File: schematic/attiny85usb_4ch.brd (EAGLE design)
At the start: 75.2 x 19 mm, 11 parts, among them IC1 PCF8574P

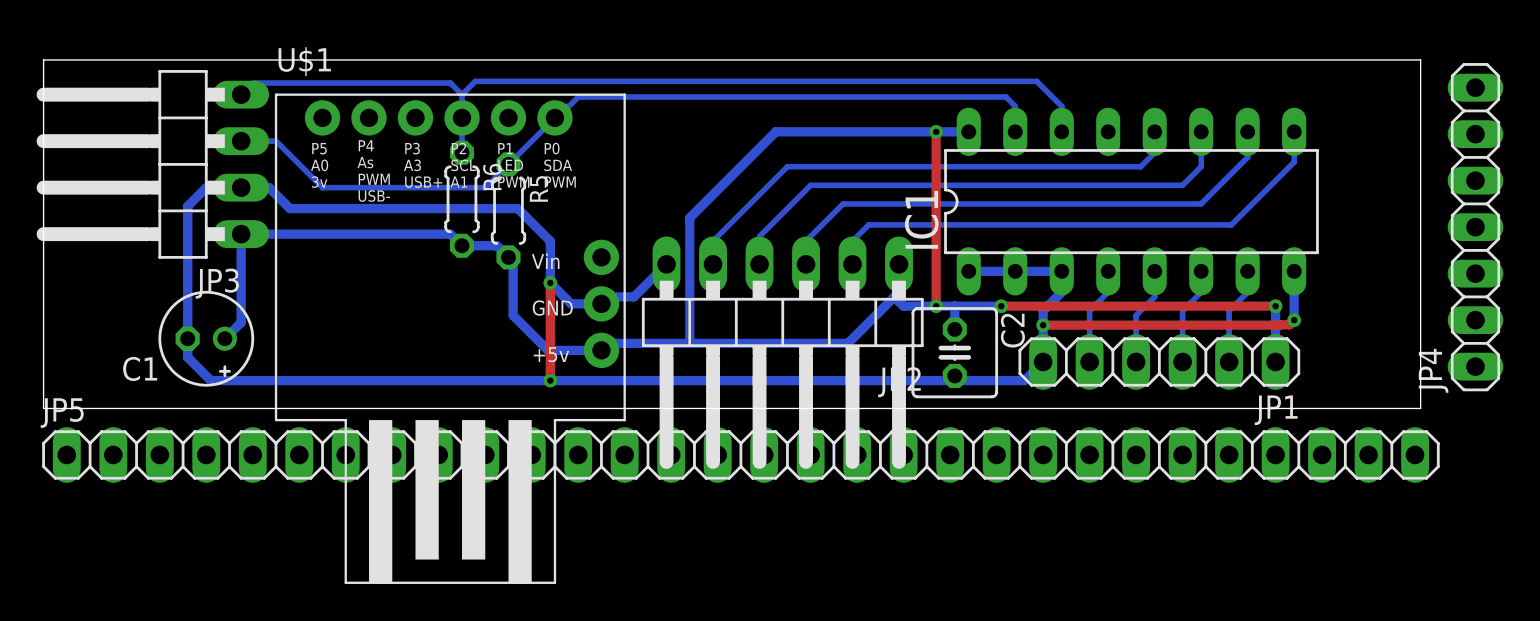
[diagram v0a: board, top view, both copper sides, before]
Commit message: update schematic
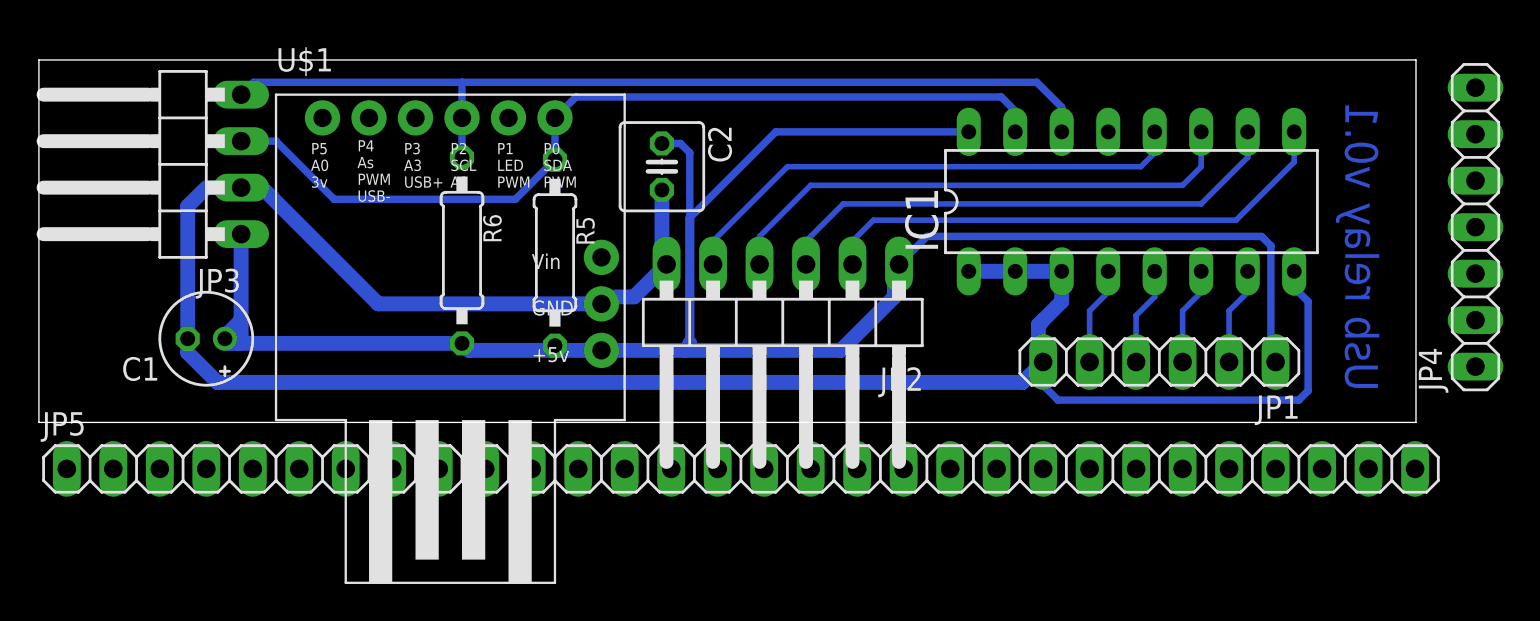
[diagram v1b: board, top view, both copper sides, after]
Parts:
- R5, R6: device rcl:0204/5 -> rcl:0207/10
- moved C2 19.0 mm to (46.5, 28.4)
- moved R5 3.42 mm to (40.6, 23.7)
- moved R6 2.79 mm to (35.6, 23.9)
- moved JP5 0.76 mm to (50.8, 11.9)
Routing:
- net GND: track 127.9 -> 137.1 mm, vias 4 -> 0
- net VCC: track 108.3 -> 105.2 mm, vias 4 -> 0
- net SCL: track 51.4 -> 54.4 mm
- net SDA: track 47.9 -> 48.7 mm
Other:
- board size 75.2 x 19 mm -> 75.2 x 19.8 mm
- board text added: "Usb relay v0.1"
